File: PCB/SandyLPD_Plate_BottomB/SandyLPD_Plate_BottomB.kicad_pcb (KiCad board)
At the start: 2 copper layers, 131 x 83 mm, 11 parts

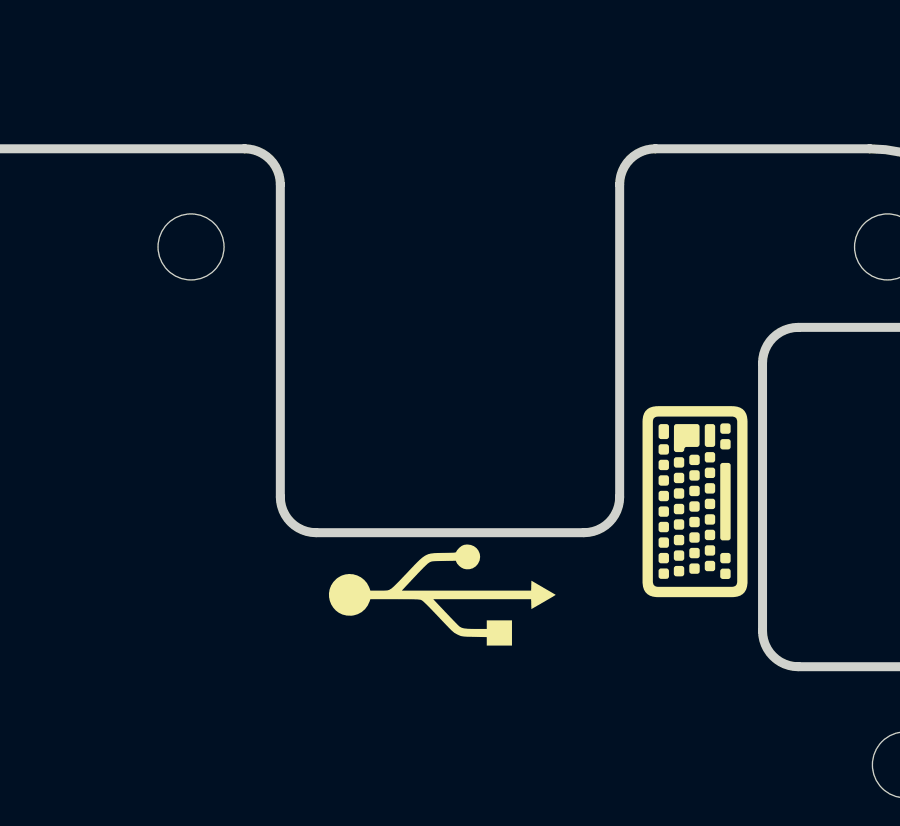
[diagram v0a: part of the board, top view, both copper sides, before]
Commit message: USBコネクタの切り欠きが大きすぎたので小さく。 #47
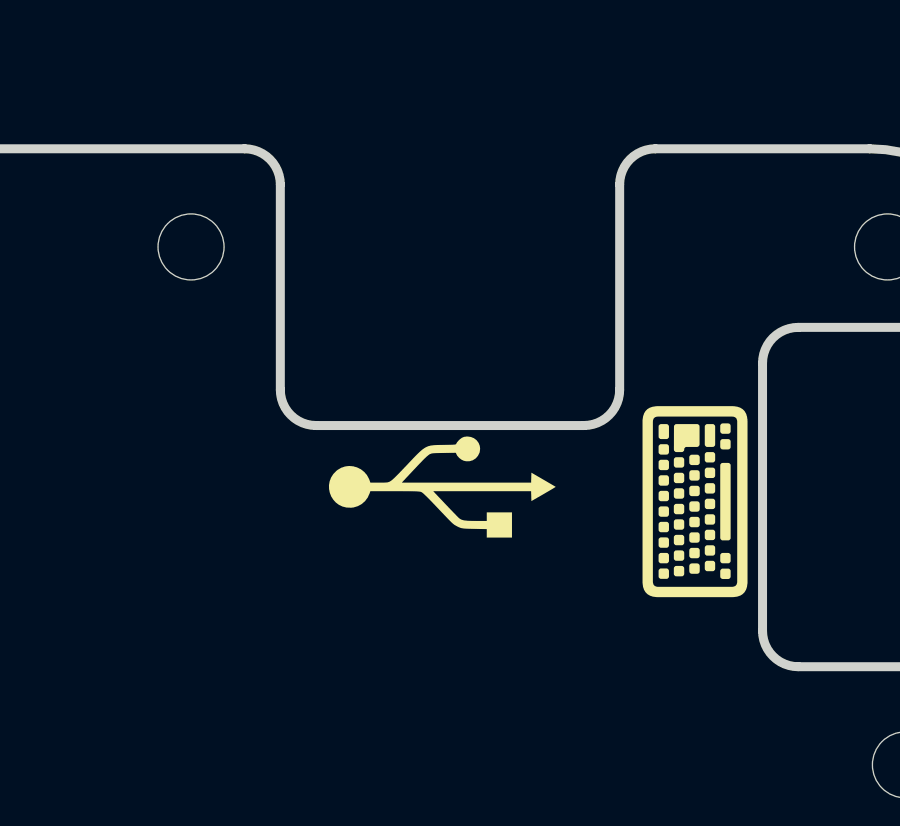
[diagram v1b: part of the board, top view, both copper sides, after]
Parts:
- moved G*** 3.60 mm to (135.4, 43.3)
- moved G*** 3.60 mm to (135.8, 43.3)
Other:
- outline, holes or cut-outs redrawn
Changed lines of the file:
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@@
 		)
 		(fp_line
-			(start -29.170337 -40.48125)
+			(start -29.170337 -44.053125)
 			(end -29.170337 -50.896915)
 			(stroke
@@
 		)
 		(fp_line
-			(start -19.05 -39.290625)
-			(end -27.979712 -39.290625)
+			(start -19.05 -42.8625)
+			(end -27.979712 -42.8625)
 			(stroke
 				(width 0.3)
@@
 		(fp_line
 			(start -17.859375 -50.896915)
-			(end -17.859375 -40.48125)
+			(end -17.859375 -44.053125)
 			(stroke
 				(width 0.3)
@@
 		)
 		(fp_arc
-			(start -27.979712 -39.290625)
-			(mid -28.821611 -39.639351)
-			(end -29.170337 -40.48125)
+			(start -27.979712 -42.8625)
+			(mid -28.821611 -43.211226)
+			(end -29.170337 -44.053125)
 			(stroke
 				(width 0.3)
@@
 		)
 		(fp_arc
-			(start -17.859375 -40.48125)
-			(mid -18.208101 -39.639351)
-			(end -19.05 -39.290625)
+			(start -17.859375 -44.053125)
+			(mid -18.208101 -43.211226)
+			(end -19.05 -42.8625)
 			(stroke
 				(width 0.3)
@@
 		)
 		(group ""
-			(members "1d8cc2c4-e88a-4503-85c8-7cdc7f5fe951" "2545b97a-3b06-4e62-a889-0e7fa287b5b0"
-				"335916c3-252b-42c0-9c90-4ce8791a3f72" "4f729eca-73d5-4b9c-949f-91c84362a6af"
-				"54e35339-30db-4bf0-be88-1a860aa4a867" "8231154a-c87d-478c-8707-29be634ed9fb"
-				"a075de65-9eec-40e8-a3e7-cc5b94b3eb27"
+			(members "275ccb09-378d-4194-afe2-ef5c4c11d279" "30e8d5e8-6227-499c-a921-2fdaba9be874"
+				"5ccf6215-889f-43fb-99c0-ea7ff10915d2" "71cac285-ff39-4f0a-a2d3-798dc5156bdc"
+				"ba9d1ee4-2b91-4e82-b0ad-5241ee355cc2" "c9f2f533-efcb-42ce-9e6d-88d1543ec91e"
+				"ce40bef5-e470-4703-95a2-ef6d0e9637db"
 			)
 		)
@@
 		(locked yes)
 		(layer "F.Cu")
-		(at 135.402185 46.928405)
+		(at 135.402185 43.328405)
 		(property "Reference" "G***"
 			(at 0 0 0)
@@
 		(locked yes)
 		(layer "B.Cu")
-		(at 135.802185 46.928405 180)
+		(at 135.802185 43.328405 180)
 		(property "Reference" "G***"
 			(at 0 0 0)

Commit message: QRコード、ロゴ追加
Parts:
- added G***: LOGO, locallib:QR_Code_SandyLP-Duo, F.Cu at (40.1, 46.1)
- added G***: LOGO, locallib:Sandy_logo_w40, F.Cu at (53.2, 91.3)
- added G***: LOGO, locallib:QR_Code_SandyLP-Duo, B.Cu at (39.9, 46.1)
- added G***: LOGO, locallib:Sandy_logo_w40, B.Cu at (53.2, 91.3)
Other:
- board text added: "https://github.com/jpskenn/SandyLP-Duo"

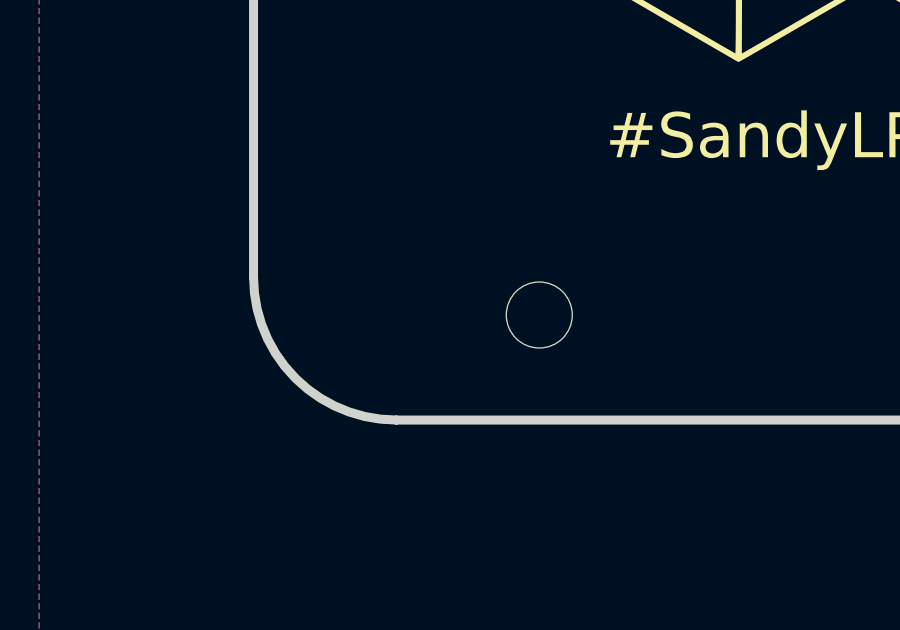
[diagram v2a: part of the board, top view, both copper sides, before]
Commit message: ネジ穴位置を再調整。
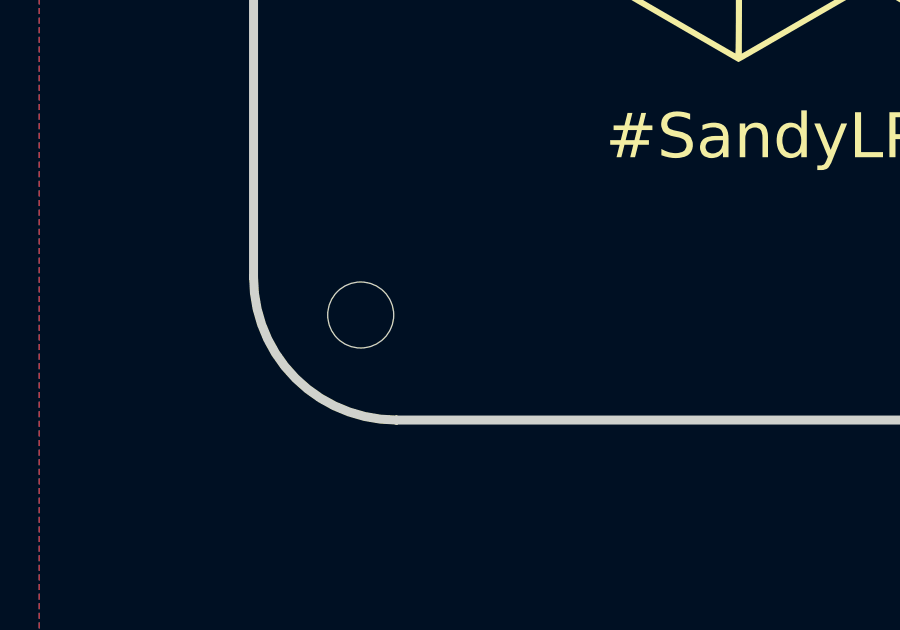
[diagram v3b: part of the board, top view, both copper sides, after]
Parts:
- moved H_btm_3 5.95 mm to (27.0, 111.5)
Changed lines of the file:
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@@
 	(footprint "locallib:MountingHole_2.2mm_M2_no_REF_Plastic_L5mm"
 		(layer "B.Cu")
-		(at 32.964693 111.537849 180)
+		(at 27.011559 111.537843 180)
 		(descr "Mounting Hole 2.2mm, no annular, M2")
 		(tags "mounting hole 2.2mm no annular m2")
